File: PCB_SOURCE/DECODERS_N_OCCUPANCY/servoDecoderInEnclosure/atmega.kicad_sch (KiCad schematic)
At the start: 9 parts, among them J3 ICSP, U202 ATmega328-A, Y201 Crystal_GND2

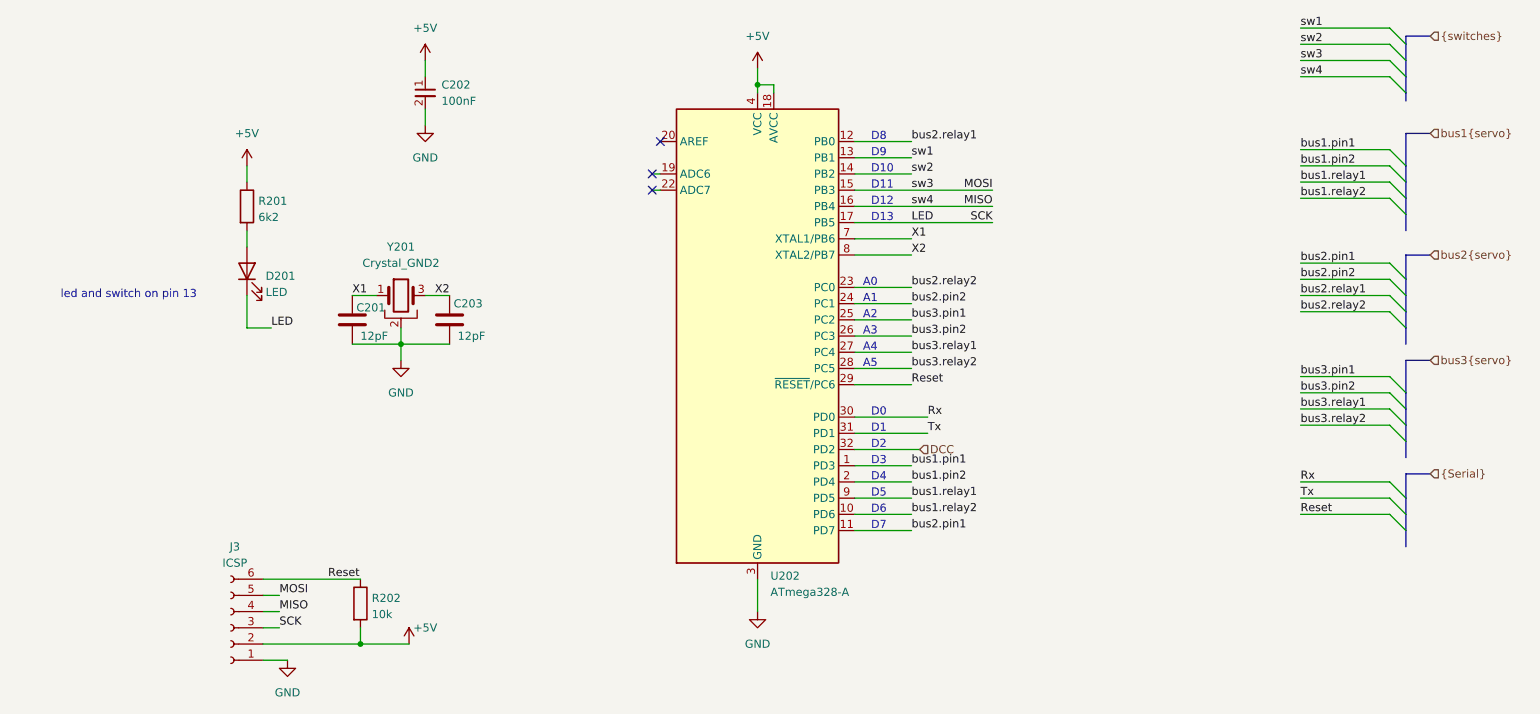
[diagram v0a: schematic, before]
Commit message: added some boards, new turning loop module with sleeper, all eating LED as well as servoDecoderInEnclosure
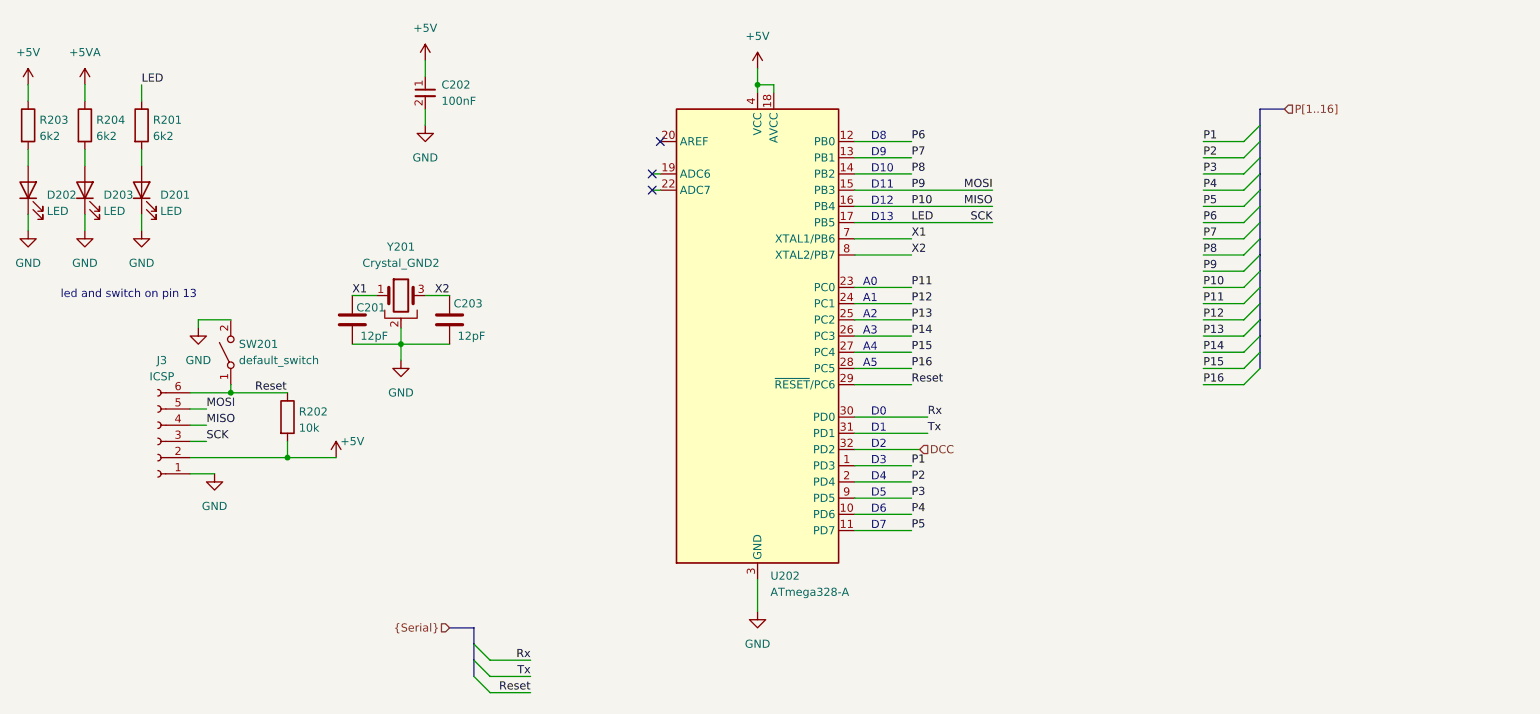
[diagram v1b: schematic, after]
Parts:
- added D202, D203: LED, LED_SMD:LED_0805_2012Metric_Pad1.15x1.40mm_HandSolder, symbol Device:LED
- added R203, R204: 6k2, Resistor_SMD:R_0603_1608Metric_Pad0.98x0.95mm_HandSolder, symbol Device:R
- added SW201: default_switch, custom_kicad_lib_sk:default_switch, symbol custom_kicad_lib_sk:default_switch
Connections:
- net +5V: now also R203.1; no longer R201.1
- net GND: now also D201.1 (K), D202.1 (K), D203.1 (K), SW201.2 (B)
- net LED: now also R201.1; no longer D201.1 (K)
- net Reset: now also SW201.1 (A)
- net bus1.pin1 renamed P1
- net bus1.pin2 renamed P2
- net bus1.relay1 renamed P3
- net bus1.relay2 renamed P4
- net bus2.pin1 renamed P5
- net bus2.pin2 renamed P12
- net bus2.relay1 renamed P6
- net bus2.relay2 renamed P11
- net bus3.pin1 renamed P13
- net bus3.pin2 renamed P14
- net bus3.relay1 renamed P15
- net bus3.relay2 renamed P16
- net sw1 renamed P7
- net sw2 renamed P8
- new net: D202.2 (A), R203.2
- new net: D203.2 (A), R204.2
- new net +5VA: R204.1
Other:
- moved on the sheet: D201, J3, R201, R202
